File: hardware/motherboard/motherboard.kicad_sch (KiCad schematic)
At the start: 72 parts, among them J1 JST-VH, J2 USB C 2.0, J3 JST-VH, J4 JST-PH, Q1 TSM7P06CP_ROG, Q2 TSM7P06CP_ROG, SW1 Boot, SW10 B, SW11 X, SW12 Y, SW2 Reset, SW3 A, SW4 B, SW5 Boot, SW6 Reset, SW7 X, SW8 Y, SW9 A, U1 ESP32-S3-WROOM-1, U2 TPS75533KTTRG3, U3 TLV75709PDBV

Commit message: Added some notes
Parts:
- added C22, C23: 1uF, symbol Device:C
- added R21, R22: 10k, symbol Device:R_US
- added SW13: Boot, symbol Switch:SW_Push
- added SW14: Reset, symbol Switch:SW_Push
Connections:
- net +3V3: now also R21.2, R22.2
- net GND: now also C22.2, C23.2, SW13.2, SW14.2
- net Select: now also C23.1, R22.1, SW14.1; no longer C15.1, R14.1, SW6.1
- net Start: now also C22.1, R21.1, SW13.1; no longer C14.1, R13.1, SW5.1
- new net BLeft: C14.1, R13.1, SW5.1
- new net BRight: C15.1, R14.1, SW6.1
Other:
- note added: "ACCs likely need voltage divider so MCU can tolerate possible communication voltage spikes up to 5V!!!!!"
- note added: "Bumper Buttons"
- note added: "Charge Status IMU (I2C: SDA/SCL)"
- note added: "IMU"
- note added: "TODO: Decide between breakout IMU or integrated on board."

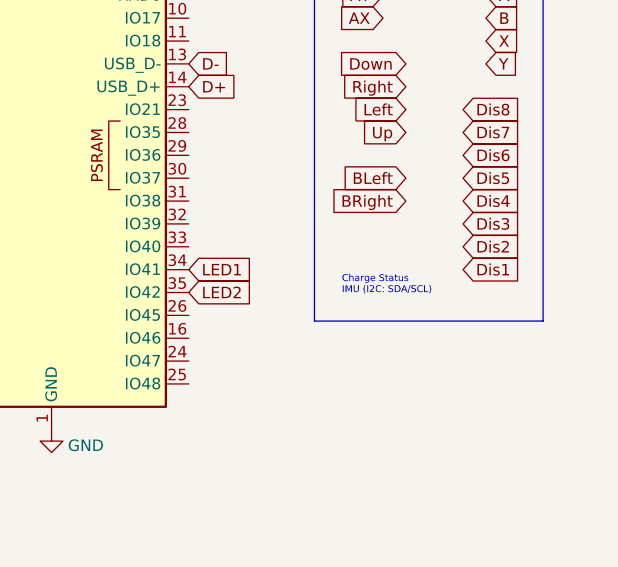
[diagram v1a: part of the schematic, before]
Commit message: Will Meeting
Added JLC constraints
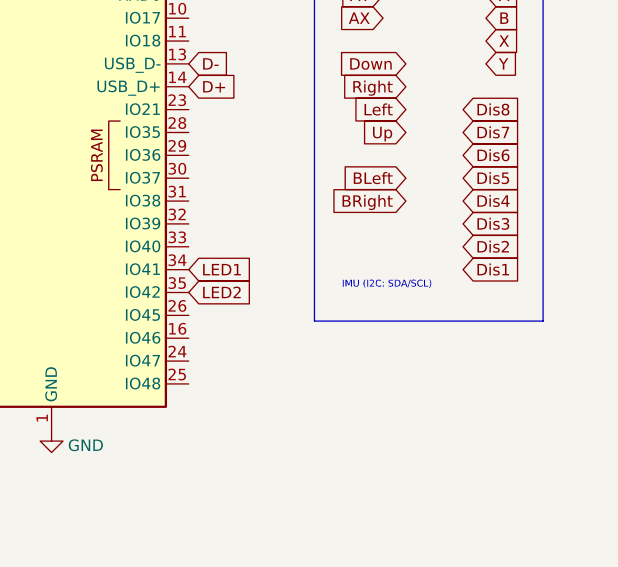
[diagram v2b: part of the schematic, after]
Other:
- note added: "IMU (I2C: SDA/SCL)"
- note removed: "Charge Status IMU (I2C: SDA/SCL)"
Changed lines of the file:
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@@
 		)
 	)
-	(text "Charge Status\nIMU (I2C: SDA/SCL)"
+	(text "IMU (I2C: SDA/SCL)"
 		(exclude_from_sim no)
 		(at 254.508 65.278 0)

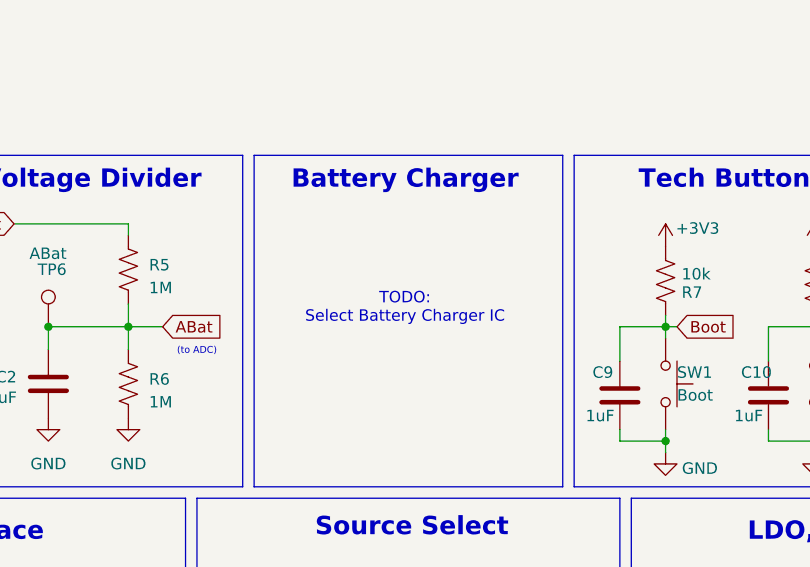
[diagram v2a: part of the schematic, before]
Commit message: Added Motherboard PCB edge cut, added some footprints
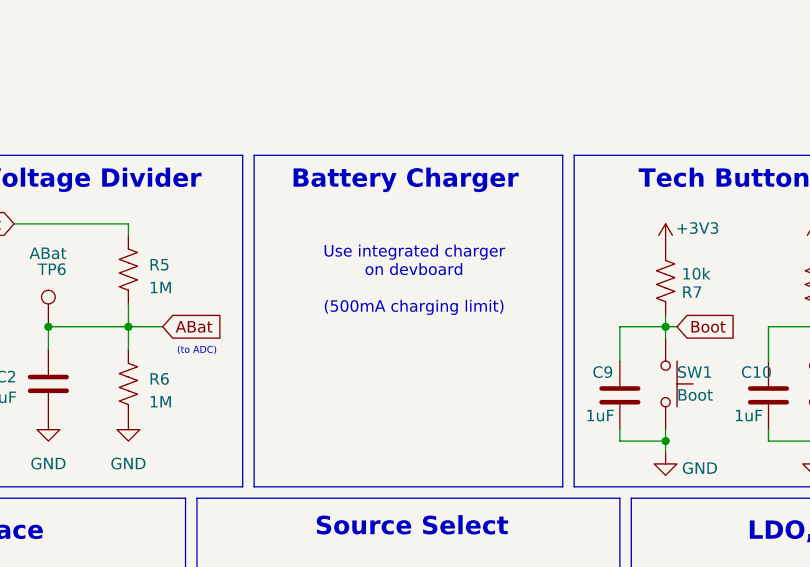
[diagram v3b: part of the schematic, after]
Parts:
- J2: footprint (none) -> Connector_USB:USB_C_Receptacle_G-Switch_GT-USB-7010ASV
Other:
- note added: "Use integrated charger on devboard (500mA charging limit)"
- note removed: "TODO: Select Battery Charger IC"
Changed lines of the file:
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@@
 		)
 	)
-	(text "TODO:\nSelect Battery Charger IC"
-		(exclude_from_sim no)
-		(at 100.584 130.048 0)
-		(effects
-			(font
-				(size 1.27 1.27)
-			)
-		)
-	)
 	(text "Voltage Divider"
 		(exclude_from_sim no)
@@
 		)
 	)
+	(text "Use integrated charger \non devboard \n\n(500mA charging limit)"
+		(exclude_from_sim no)
+		(at 101.6 127 0)
+		(effects
+			(font
+				(size 1.27 1.27)
+			)
+		)
+	)
 	(text "IMU"
 		(exclude_from_sim no)
@@
 			)
 		)
-		(property "Footprint" ""
+		(property "Footprint" "Connector_USB:USB_C_Receptacle_G-Switch_GT-USB-7010ASV"
 			(at 50.8 177.8 0)
 			(effects

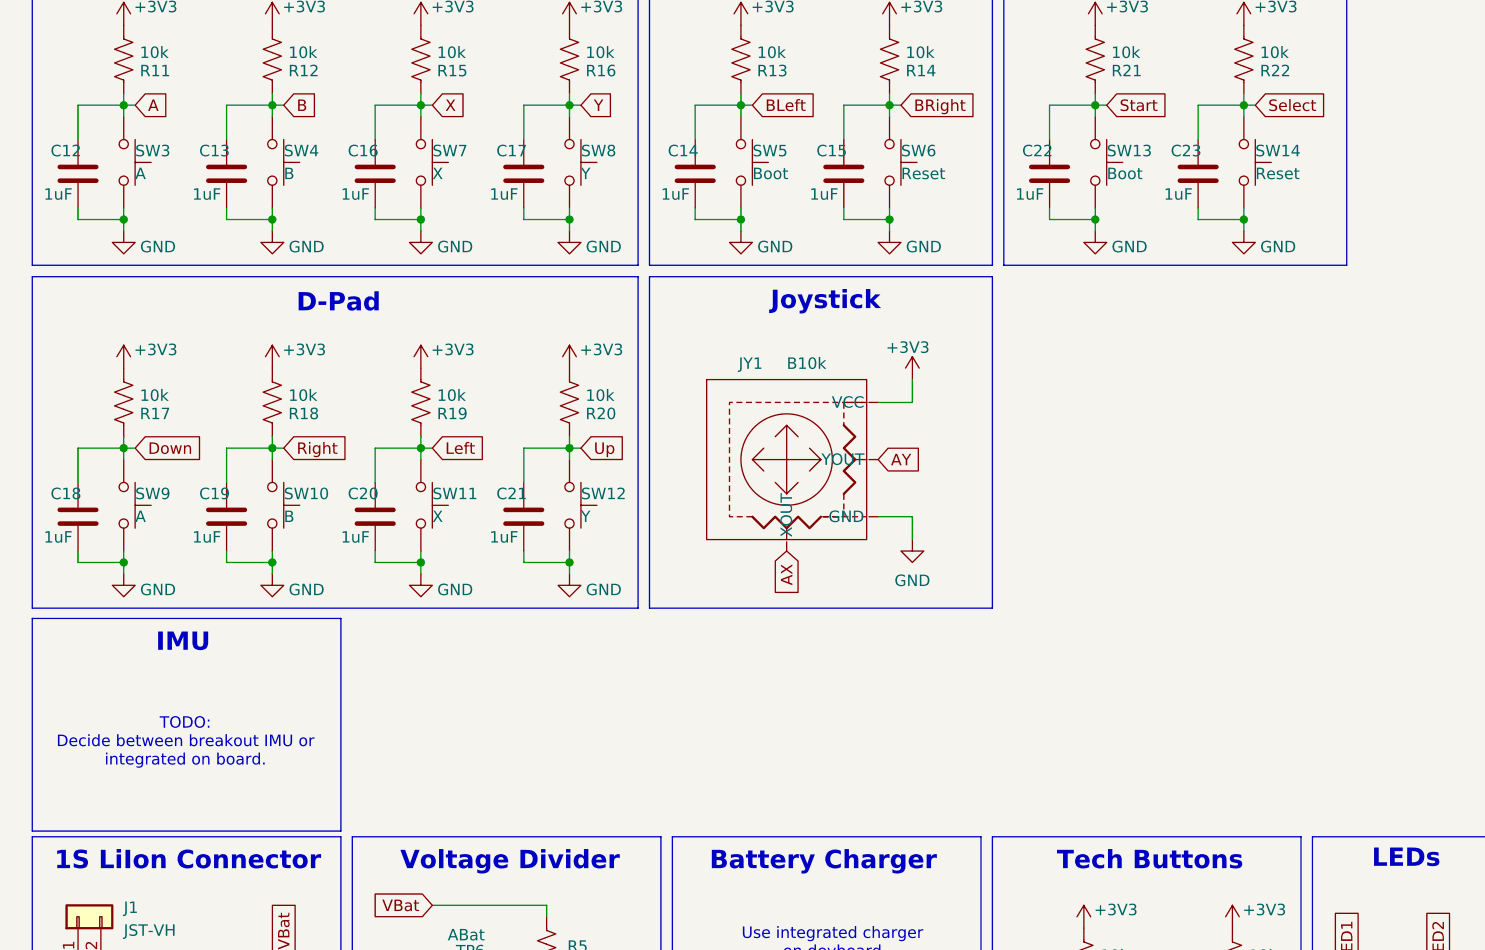
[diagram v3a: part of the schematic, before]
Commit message: Added footprints in motherboard, preparing for PCB layout
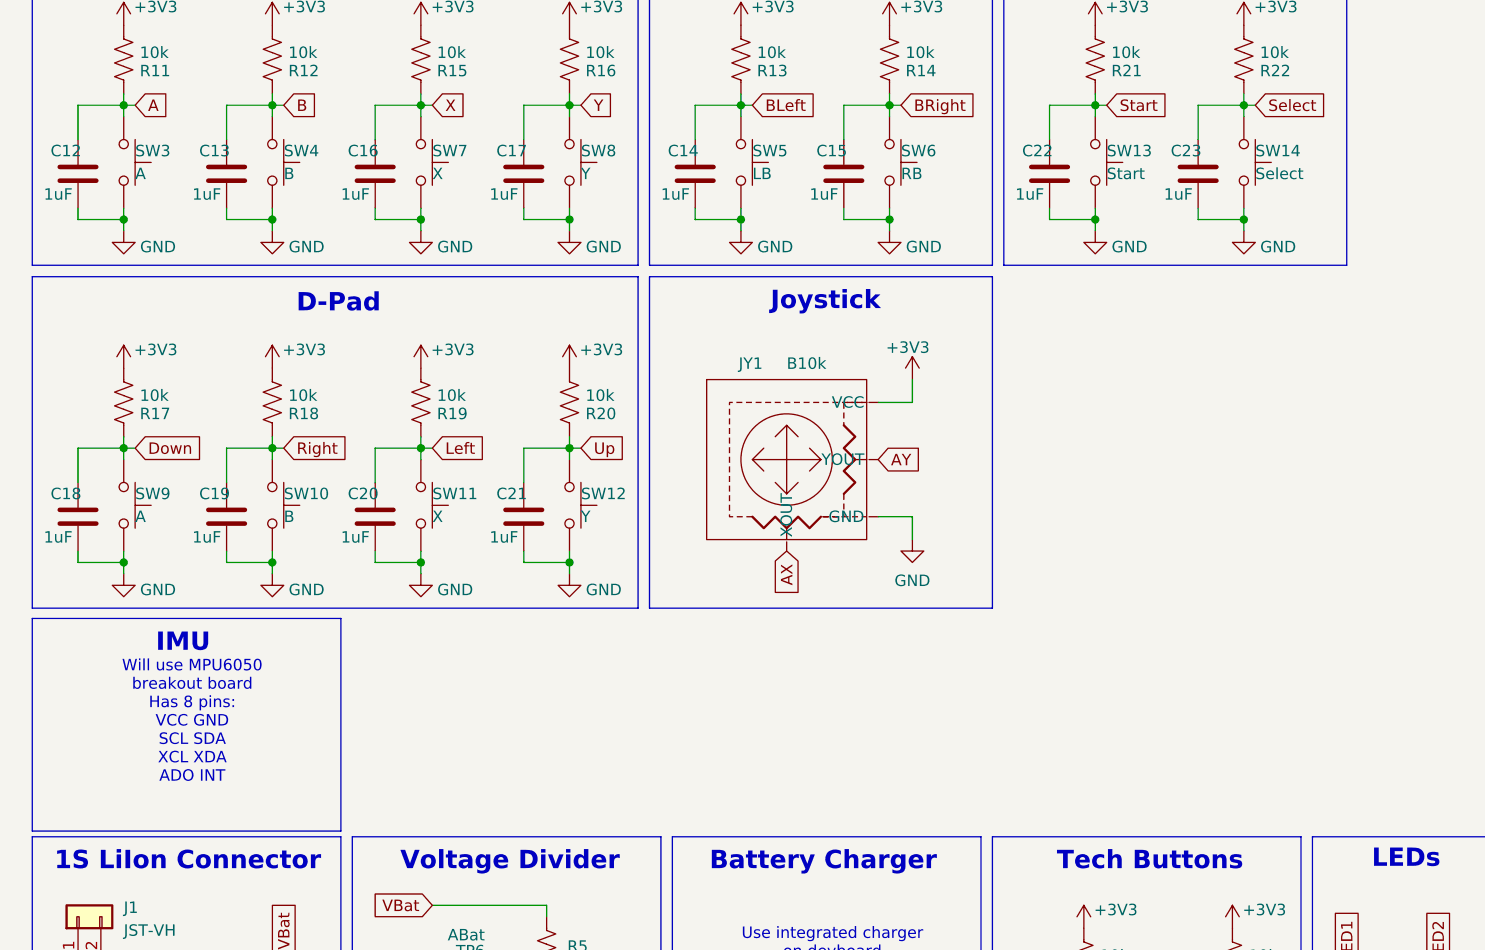
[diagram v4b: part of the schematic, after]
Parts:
- C12, C13, C14, C15, C16, C17, C18, C19, C20, C21, C22, C23: footprint (none) -> Capacitor_SMD:C_0201_0603Metric
- D1: footprint VS15AWL06FNTRM3 -> esp32_handheld:DPAK_Q03FN-M3_VIS
- J1: footprint (none) -> Connector_JST:JST_VH_B2P-VH-FB-B_1x02_P3.96mm_Vertical
- J3: footprint (none) -> Connector_JST:JST_VH_B2PS-VH_1x02_P3.96mm_Horizontal
- J4: footprint (none) -> Connector_JST:JST_PH_B8B-PH-SM4-TB_1x08-1MP_P2.00mm_Vertical
- Q1, Q2: footprint TSM7P06CPROG -> esp32_handheld:TRANS_TSM7P06CP_ROG
- R10, R11, R12, R13, R14, R15, R16, R17, R18, R19, R20, R21, R22, R7, R8, R9: footprint (none) -> Resistor_SMD:R_0603_1608Metric
- SW13: value Boot -> Start
- SW14: value Reset -> Select
- SW5: value Boot -> LB
- SW6: value Reset -> RB
- TP1, TP2, TP3, TP4, TP5, TP6: footprint (none) -> TestPoint:TestPoint_Pad_D1.5mm
- U2: footprint KTT5_6P22X6P86 -> esp32_handheld:KTT5_6P22X6P86
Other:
- note added: "Will use MPU6050 breakout board Has 8 pins: VCC GND SCL SDA XCL XDA ADO INT"
- note removed: "TODO: Decide between breakout IMU or integrated on board."
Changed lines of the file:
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@@
 		)
 	)
-	(text "TODO:\nDecide between breakout IMU or\nintegrated on board."
+	(text "Will use MPU6050\nbreakout board \nHas 8 pins:\nVCC GND\nSCL SDA\nXCL XDA\nADO INT"
 		(exclude_from_sim no)
-		(at 29.718 102.616 0)
+		(at 30.48 100.33 0)
 		(effects
 			(font
@@
 			)
 		)
-		(property "Footprint" ""
+		(property "Footprint" "Capacitor_SMD:C_0201_0603Metric"
 			(at 35.2552 43.18 0)
 			(effects
@@
 			)
 		)
-		(property "Footprint" ""
+		(property "Footprint" "Resistor_SMD:R_0603_1608Metric"
 			(at 71.374 26.416 90)
 			(effects
@@
 			)
 		)
-		(property "Footprint" "TSM7P06CPROG"
+		(property "Footprint" "esp32_handheld:TRANS_TSM7P06CP_ROG"
 			(at 199.06 165.1 0)
 			(effects
@@
 			)
 		)
-		(property "Value" "Reset"
+		(property "Value" "Select"
 			(at 148.59 39.37 90)
 			(effects
@@
 			)
 		)
-		(property "Footprint" ""
+		(property "Footprint" "Resistor_SMD:R_0603_1608Metric"
 			(at 71.374 64.516 90)
 			(effects
@@
 			)
 		)
-		(property "Footprint" ""
+		(property "Footprint" "Resistor_SMD:R_0603_1608Metric"
 			(at 38.354 64.516 90)
 			(effects
@@
 			)
 		)
-		(property "Footprint" ""
+		(property "Footprint" "TestPoint:TestPoint_Pad_D1.5mm"
 			(at 35.56 139.7 0)
 			(effects
@@
 			)
 		)
-		(property "Footprint" ""
+		(property "Footprint" "Resistor_SMD:R_0603_1608Metric"
 			(at 145.034 126.746 90)
 			(effects
@@
 			)
 		)
-		(property "Footprint" ""
+		(property "Footprint" "TestPoint:TestPoint_Pad_D1.5mm"
 			(at 17.78 144.78 0)
 			(effects
@@
 			)
 		)
-		(property "Footprint" ""
+		(property "Footprint" "Capacitor_SMD:C_0201_0603Metric"
 			(at 68.2752 81.28 0)
 			(effects
@@
 			)
 		)
-		(property "Footprint" ""
+		(property "Footprint" "Connector_JST:JST_VH_B2P-VH-FB-B_1x02_P3.96mm_Vertical"
 			(at 17.78 121.92 0)
 			(effects
@@
 			)
 		)
-		(property "Footprint" ""
+		(property "Footprint" "TestPoint:TestPoint_Pad_D1.5mm"
 			(at 163.83 161.29 0)
 			(effects
@@
 			)
 		)
-		(property "Footprint" ""
+		(property "Footprint" "TestPoint:TestPoint_Pad_D1.5mm"
 			(at 66.04 132.08 0)
 			(effects
@@
 			)
 		)
-		(property "Footprint" ""
+		(property "Footprint" "Resistor_SMD:R_0603_1608Metric"
 			(at 90.424 26.416 90)
 			(effects
@@
 			)
 		)
-		(property "Footprint" ""
+		(property "Footprint" "Resistor_SMD:R_0603_1608Metric"
 			(at 146.304 26.416 90)
 			(effects
@@
 			)
 		)
-		(property "Footprint" ""
+		(property "Footprint" "Capacitor_SMD:C_0201_0603Metric"
 			(at 87.3252 43.18 0)
 			(effects
@@
 			)
 		)
-		(property "Footprint" ""
+		(property "Footprint" "Capacitor_SMD:C_0201_0603Metric"
 			(at 68.2752 43.18 0)
 			(effects
@@
 			)
 		)
-		(property "Footprint" ""
+		(property "Footprint" "Resistor_SMD:R_0603_1608Metric"
 			(at 128.524 126.746 90)
 			(effects
@@
 			)
 		)
-		(property "Footprint" ""
+		(property "Footprint" "Capacitor_SMD:C_0201_0603Metric"
 			(at 18.7452 81.28 0)
 			(effects
@@
 			)
 		)
-		(property "Footprint" ""
+		(property "Footprint" "Capacitor_SMD:C_0201_0603Metric"
 			(at 51.7652 81.28 0)
 			(effects
@@
 			)
 		)
-		(property "Footprint" ""
+		(property "Footprint" "Connector_JST:JST_PH_B8B-PH-SM4-TB_1x08-1MP_P2.00mm_Vertical"
 			(at 267.97 147.32 0)
 			(effects
@@
 			)
 		)
-		(property "Footprint" ""
+		(property "Footprint" "Resistor_SMD:R_0603_1608Metric"
 			(at 157.734 139.446 90)
 			(effects
@@
 			)
 		)
-		(property "Footprint" ""
+		(property "Footprint" "Connector_JST:JST_VH_B2PS-VH_1x02_P3.96mm_Horizontal"
 			(at 245.11 140.97 0)
 			(effects
@@
 			)
 		)
-		(property "Footprint" ""
+		(property "Footprint" "Capacitor_SMD:C_0201_0603Metric"
 			(at 103.8352 43.18 0)
 			(effects
@@
 			)
 		)
-		(property "Footprint" ""
+		(property "Footprint" "Resistor_SMD:R_0603_1608Metric"
 			(at 167.894 139.446 90)
 			(effects
@@
 			)
 		)
-		(property "Footprint" "KTT5_6P22X6P86"
+		(property "Footprint" "esp32_handheld:KTT5_6P22X6P86"
 			(at 183.896 131.064 0)
 			(effects
@@
 			)
 		)
-		(property "Footprint" ""
+		(property "Footprint" "Capacitor_SMD:C_0201_0603Metric"
 			(at 143.2052 43.18 0)
 			(effects
@@
 			)
 		)
-		(property "Footprint" ""
+		(property "Footprint" "Capacitor_SMD:C_0201_0603Metric"
 			(at 51.7652 43.18 0)
 			(effects
@@
 			)
 		)
-		(property "Footprint" ""
+		(property "Footprint" "Resistor_SMD:R_0603_1608Metric"
 			(at 21.844 64.516 90)
 			(effects
@@
 			)
 		)
-		(property "Footprint" ""
+		(property "Footprint" "Resistor_SMD:R_0603_1608Metric"
 			(at 129.794 26.416 90)
 			(effects
@@
 			)
 		)
-		(property "Footprint" ""
+		(property "Footprint" "Resistor_SMD:R_0603_1608Metric"
 			(at 21.844 26.416 90)
 			(effects
@@
 			)
 		)
-		(property "Footprint" ""
+		(property "Footprint" "Resistor_SMD:R_0603_1608Metric"
 			(at 106.934 26.416 90)
 			(effects
@@
 			)
 		)
-		(property "Footprint" "TSM7P06CPROG"
+		(property "Footprint" "esp32_handheld:TRANS_TSM7P06CP_ROG"
 			(at 131.75 130.81 0)
 			(effects
@@
 			)
 		)
-		(property "Value" "Reset"
+		(property "Value" "RB"
 			(at 109.22 39.37 90)
 			(effects
@@
 			)
 		)
-		(property "Footprint" ""
+		(property "Footprint" "Resistor_SMD:R_0603_1608Metric"
 			(at 54.864 64.516 90)
 			(effects
@@
 			)
 		)
-		(property "Footprint" ""
+		(property "Footprint" "TestPoint:TestPoint_Pad_D1.5mm"
 			(at 226.06 148.59 0)
 			(effects
@@
 			)
 		)
-		(property "Footprint" ""
+		(property "Footprint" "TestPoint:TestPoint_Pad_D1.5mm"
 			(at 119.38 161.29 0)
 			(effects
@@
 			)
 		)
-		(property "Footprint" ""
+		(property "Footprint" "Capacitor_SMD:C_0201_0603Metric"
 			(at 35.2552 81.28 0)
 			(effects
@@
 			)
 		)
-		(property "Footprint" ""
+		(property "Footprint" "Capacitor_SMD:C_0201_0603Metric"
 			(at 126.6952 43.18 0)
 			(effects
@@
 			)
 		)
-		(property "Footprint" ""
+		(property "Footprint" "Resistor_SMD:R_0603_1608Metric"
 			(at 38.354 26.416 90)
 			(effects
@@
 			)
 		)
-		(property "Footprint" ""
+		(property "Footprint" "Capacitor_SMD:C_0201_0603Metric"
 			(at 18.7452 43.18 0)
 			(effects
@@
 			)
 		)
-		(property "Footprint" "VS15AWL06FNTRM3"
+		(property "Footprint" "esp32_handheld:DPAK_Q03FN-M3_VIS"
 			(at 121.92 273.99 0)
 			(effects
@@
 			)
 		)
-		(property "Footprint" ""
+		(property "Footprint" "Resistor_SMD:R_0603_1608Metric"
 			(at 54.864 26.416 90)
 			(effects
@@
 			)
 		)
-		(property "Value" "Boot"
+		(property "Value" "LB"
 			(at 92.71 39.37 90)
 			(effects
@@
 			)
 		)
-		(property "Value" "Boot"
+		(property "Value" "Start"
 			(at 132.08 39.37 90)
 			(effects
